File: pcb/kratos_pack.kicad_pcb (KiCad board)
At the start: 4 copper layers, 42.2 x 18.6 mm, 119 parts, among them J1 USB_C_Receptacle_USB2.0, J2 PROG_CONN_STM_6p, J3 DBG_UART, J5 BAT_7.4V, J6 BAT_0V, J7 OUT+, J8 OUT-, Q1 AON7403, Q2 AON7414, Q3 AON7414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

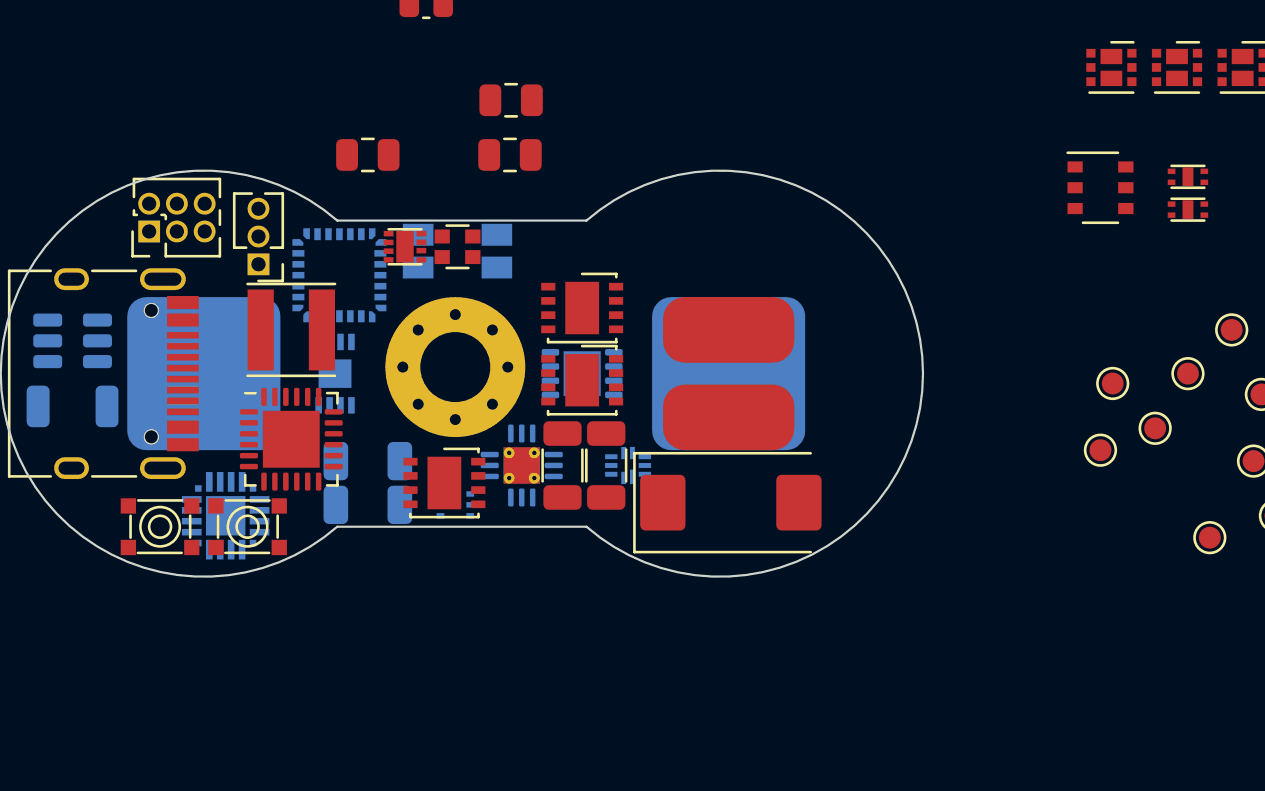
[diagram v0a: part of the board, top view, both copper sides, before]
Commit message: Schema: update footprint 3-pin connectors, project cleanup, add gitignore
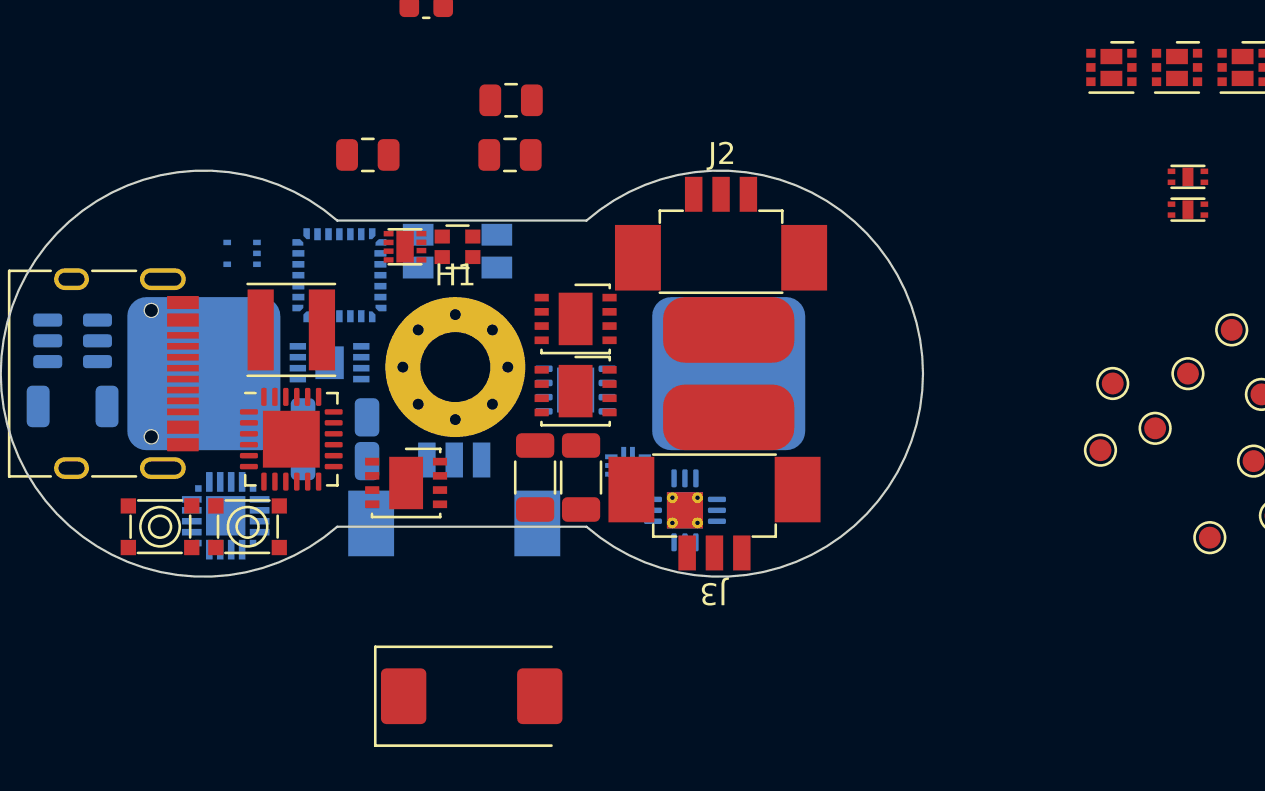
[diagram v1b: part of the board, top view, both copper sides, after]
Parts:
- removed U12: 74LVC2G14, Package_SO:TSOP-6_1.65x3.05mm_P0.95mm
- added J4: BAT_MID+NTC, TCY_connectors:Amphenol_10114828-11103LF_1x03_P1.25mm_Vertical, B.Cu at (151.4, 84.7)
- C22, C24: value 4.7uF(X7R) -> 4.7uF
- C23, C9: value 40nF -> 39nF
- J2: value PROG_CONN_STM_6p -> PROG_CONN; footprint Connector_PinHeader_1.27mm:PinHeader_2x03_P1.27mm_Vertical -> TCY_connectors:Amphenol_10114828-11103LF_1x03_P1.25mm_Vertical
- J3: footprint Connector_PinHeader_1.27mm:PinHeader_1x03_P1.27mm_Vertical -> TCY_connectors:Amphenol_10114828-11103LF_1x03_P1.25mm_Vertical
- moved J2 26.2 mm to (163.7, 72.5), turned to 0 degrees
- moved J3 24.3 mm to (163.3, 87.5)
- moved U6 15.1 mm to (141.8, 74.5)
- moved C17 14.8 mm to (152.2, 94.8)
- moved U8 7.74 mm to (162.0, 86.2)
- moved R23 2.50 mm to (146.0, 82.0)
- moved R24 2.50 mm to (146.0, 84.0)
- moved Q1 1.75 mm to (149.2, 85.0)
- moved R28 1.37 mm to (155.2, 84.8)
- moved R29 1.27 mm to (157.2, 84.8)
- moved U9 0.81 mm to (157.0, 80.8)
- moved Q2 0.58 mm to (157.0, 80.8)
- moved Q3 0.58 mm to (157.0, 77.5)
- moved U10 0.56 mm to (145.8, 79.5), turned to 0 degrees
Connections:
- J1 pad A8: no_connect_82 -> no_connect_81
- J1 pad B8: no_connect_83 -> no_connect_82
- J2 pad 2: +3V3 -> /SWCLK
- J2 pad 3: no_connect_84 -> /SWDIO
- Q4 pad 3: /DIV_1 -> /DIV_2
- Q5 pad 3: /DIV -> /DIV_1
- Q6 pad 3: /DIV_2 -> /DIV
- R16 pad 1: /DIV_2 -> /DIV
- R3 pad 1: /DIV_1 -> /DIV_2
- R8 pad 1: /DIV -> /DIV_1
- U2 pad 1: no_connect_85 -> no_connect_83
- U2 pad 10: no_connect_86 -> (no net)
- U2 pad 11: no_connect_87 -> no_connect_84
- U2 pad 14: no_connect_88 -> no_connect_85
- U2 pad 15: no_connect_89 -> no_connect_86
- U2 pad 16: no_connect_90 -> no_connect_87
- U2 pad 19: no_connect_91 -> no_connect_88
- U2 pad 2: no_connect_92 -> no_connect_89
- U2 pad 20: no_connect_93 -> no_connect_90
- U3 pad 1: no_connect_94 -> no_connect_91
- U3 pad 10: no_connect_95 -> no_connect_92
- U3 pad 11: no_connect_96 -> no_connect_93
- U3 pad 12: no_connect_97 -> no_connect_94
- U3 pad 13: no_connect_98 -> no_connect_95
- U3 pad 14: no_connect_99 -> no_connect_96
- U3 pad 15: no_connect_100 -> no_connect_97
- U3 pad 16: no_connect_101 -> no_connect_98
- U3 pad 17: no_connect_102 -> no_connect_99
- U3 pad 18: no_connect_103 -> no_connect_100
- U3 pad 19: no_connect_104 -> no_connect_101
- U3 pad 2: no_connect_105 -> no_connect_102
- U3 pad 20: no_connect_106 -> no_connect_103
- U3 pad 22: no_connect_107 -> no_connect_104
- U3 pad 23: no_connect_108 -> no_connect_105
- U3 pad 24: no_connect_109 -> no_connect_106
- U3 pad 25: no_connect_110 -> no_connect_107
- U3 pad 26: no_connect_111 -> no_connect_108
- U3 pad 27: no_connect_112 -> no_connect_109
- U3 pad 28: no_connect_113 -> no_connect_110
- U3 pad 6: no_connect_114 -> no_connect_111
- U3 pad 7: no_connect_115 -> no_connect_112
- U3 pad 8: no_connect_116 -> no_connect_113
- U3 pad 9: no_connect_117 -> no_connect_114
- U4 pad 1: no_connect_118 -> no_connect_115
- U7 pad 8: Net-(U7-Pad8) -> GND

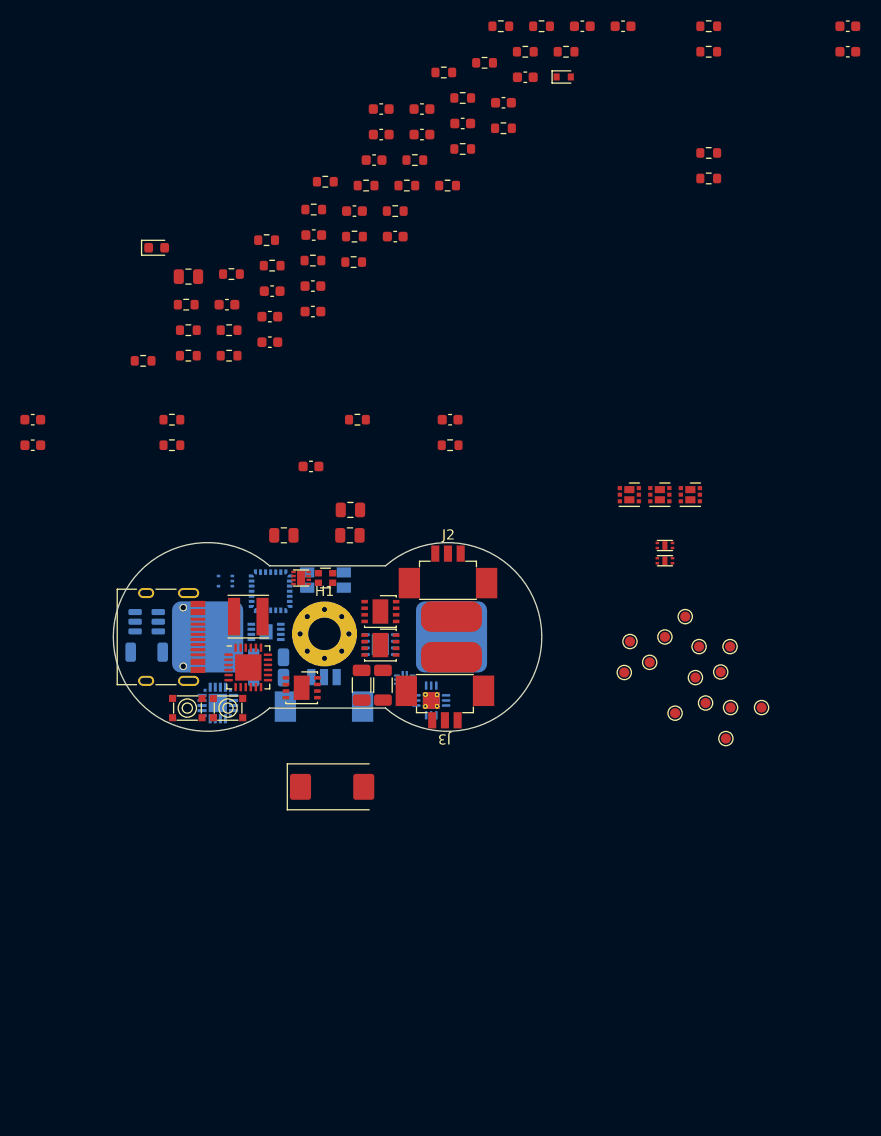
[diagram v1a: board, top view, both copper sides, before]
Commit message: PCB: Route USB input, charger circuit and switches
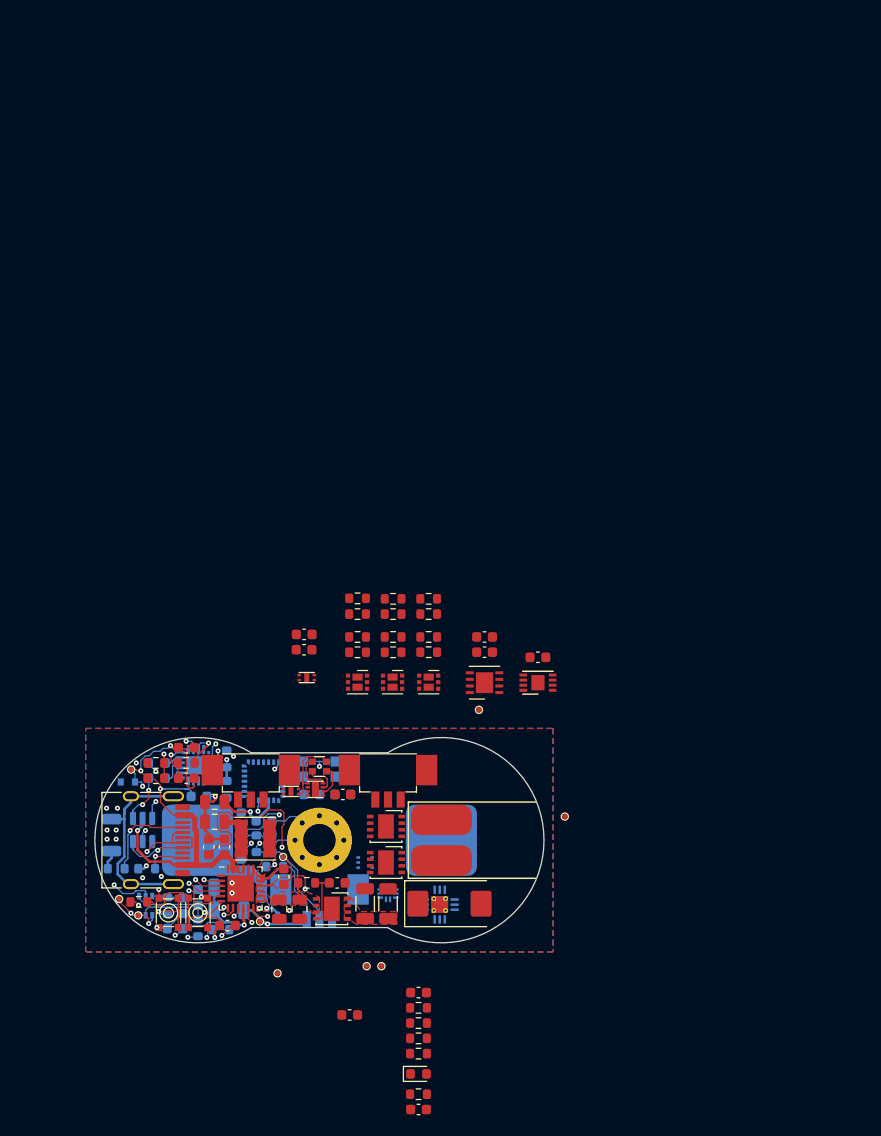
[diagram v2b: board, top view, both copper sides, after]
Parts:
- removed C15: 100nF, Capacitor_SMD:C_0603_1608Metric
- removed C2: 4.7uF, Capacitor_SMD:C_0603_1608Metric
- removed TP11, TP13: TestPoint, TestPoint:TestPoint_Pad_D1.0mm
- added U12: 74LVC2G14, Package_TO_SOT_SMD:SOT-363_SC-70-6, B.Cu at (133.9, 106.5)
- C1, C13, C27, C28, C29, C30, C4, D1, R1, R10, R11, R12, R13, R18, R2, R20, R21, R22, R35, R36, R5, R6: moved to B.Cu
- TP1, TP3: footprint TestPoint:TestPoint_Pad_D1.0mm -> TCY_connectors:TestPoint_Pad_D0.5mm; moved to B.Cu
- TP10, TP12, TP14, TP2, TP4, TP5, TP6, TP7, TP8, TP9: footprint TestPoint:TestPoint_Pad_D1.0mm -> TCY_connectors:TestPoint_Pad_D0.5mm
- U10, U9: moved to F.Cu
- moved R25 97.7 mm to (160.8, 121.0)
- moved C23 96.0 mm to (160.8, 126.5)
- moved C29 90.5 mm to (153.3, 95.5), turned to 180 degrees
- moved C30 90.1 mm to (150.2, 95.5)
- moved C5 89.8 mm to (141.7, 100.7), turned to 90 degrees
- moved C10 88.5 mm to (141.9, 108.4)
- moved R21 86.4 mm to (143.3, 101.1), turned to 90 degrees
- moved D3 85.3 mm to (160.8, 123.0)
- moved R19 84.2 mm to (133.2, 106.1)
- moved C3 83.6 mm to (137.9, 93.9)
- moved R32 82.1 mm to (160.8, 125.0)
- moved R14 82.1 mm to (134.9, 93.9)
- moved D1 81.6 mm to (132.2, 94.3), turned to 180 degrees
- moved R20 80.7 mm to (143.3, 98.1), turned to -90 degrees
- moved R15 80.1 mm to (134.9, 92.4), turned to 180 degrees
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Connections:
- Q5 pad 3: /DIV_1 -> /DIV
- Q6 pad 3: /DIV -> /DIV_1
- R16 pad 1: /DIV -> /DIV_1
- R35 pad 2: /WAKEUP -> /IN
- R36 pad 2: /BOOTL -> /IN_1
- R8 pad 1: /DIV_1 -> /DIV
- SW1 pad 2: /OUT -> /IN
- SW2 pad 2: /OUT_1 -> /IN_1
- TP12 pad 1: /OUT -> /WAKEUP
- TP14 pad 1: /OUT_1 -> /BOOTL
- TP2 pad 1: Net-(C2-Pad1) -> VBUS
- U2 pad 10: (no net) -> no_connect_116
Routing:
- net VBUS: track 0.00 -> 52.6 mm, vias 0 -> 5
- net GND: track 0.00 -> 51.7 mm, vias 0 -> 22
- net +3V3: track 0.00 -> 42.8 mm, vias 0 -> 2
- net /BOOTL: track 0.00 -> 28.7 mm, vias 0 -> 2
- net /IN: track 0.00 -> 28.4 mm, vias 0 -> 2
- net Net-(C8-Pad2): track 0.00 -> 27.4 mm, vias 0 -> 2
- net /USB_DET: track 0.00 -> 24.7 mm, vias 0 -> 3
- net /TS: track 0.00 -> 21.4 mm, vias 0 -> 2
- net Net-(FB1-Pad1): track 0.00 -> 19.9 mm
- net /RESET: track 0.00 -> 18.8 mm, vias 0 -> 2
- net /CH_STAT: track 0.00 -> 17.1 mm, vias 0 -> 2
- net /SCL: track 0.00 -> 16.9 mm, vias 0 -> 1
- net /CH_INT: track 0.00 -> 16.8 mm, vias 0 -> 1
- net /B1_V: track 0.00 -> 16.5 mm, vias 0 -> 1
- net /SDA: track 0.00 -> 14.4 mm, vias 0 -> 1
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- added copper zone on B.Cu, net /B2_V
- added copper zone on F.Cu, net /B2_V
- added copper zone on F.Cu, net /VBAT
- added copper zone on B.Cu, net GND
- added copper zone on F.Cu, net GND
- added copper zone on In1.Cu, net GND
- added copper zone on In2.Cu, net GND
- added copper zone on F.Cu, net Net-(C7-Pad1)
- added copper zone on F.Cu, net Net-(C9-Pad2)
- added copper zone on F.Cu, net VCC
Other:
- board size 42.2 x 18.6 mm -> 44.2 x 20.2 mm

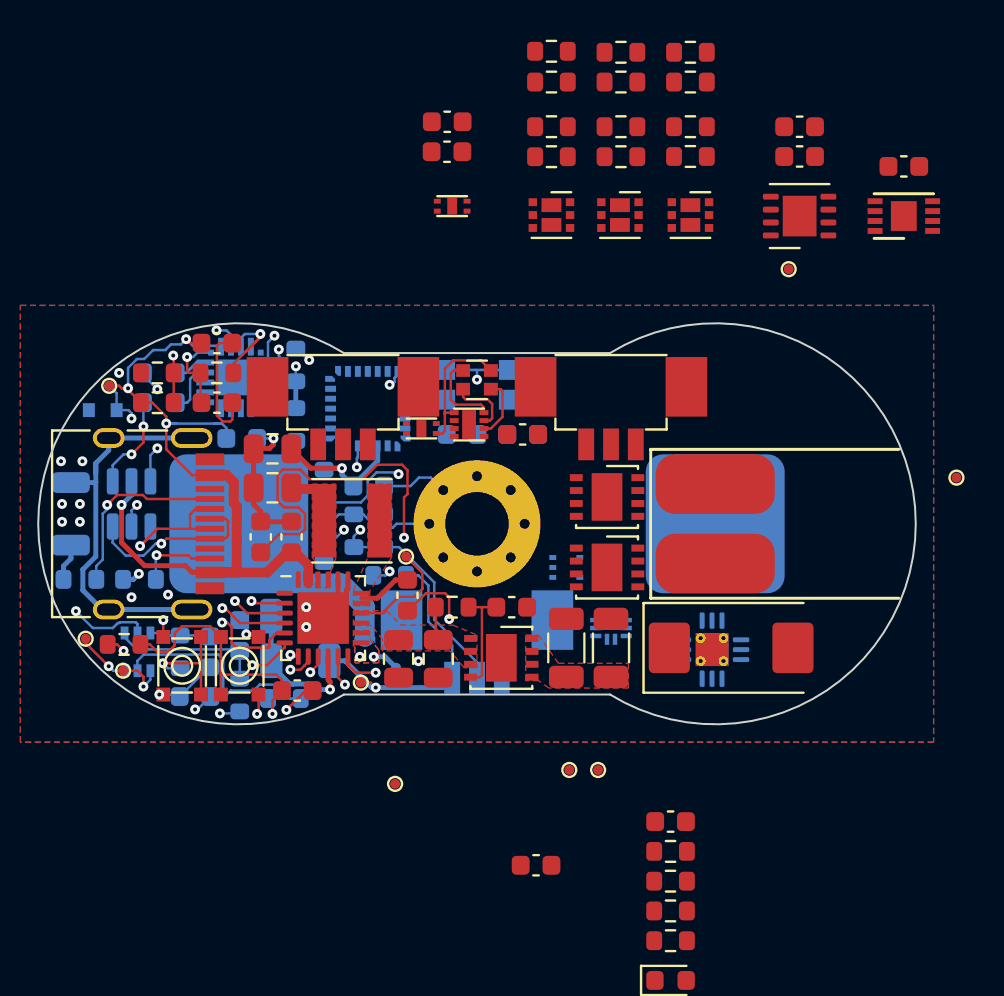
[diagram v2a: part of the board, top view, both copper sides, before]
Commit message: PCB: routing of mcu, voltage mesuring, part of current sensing and power regulator
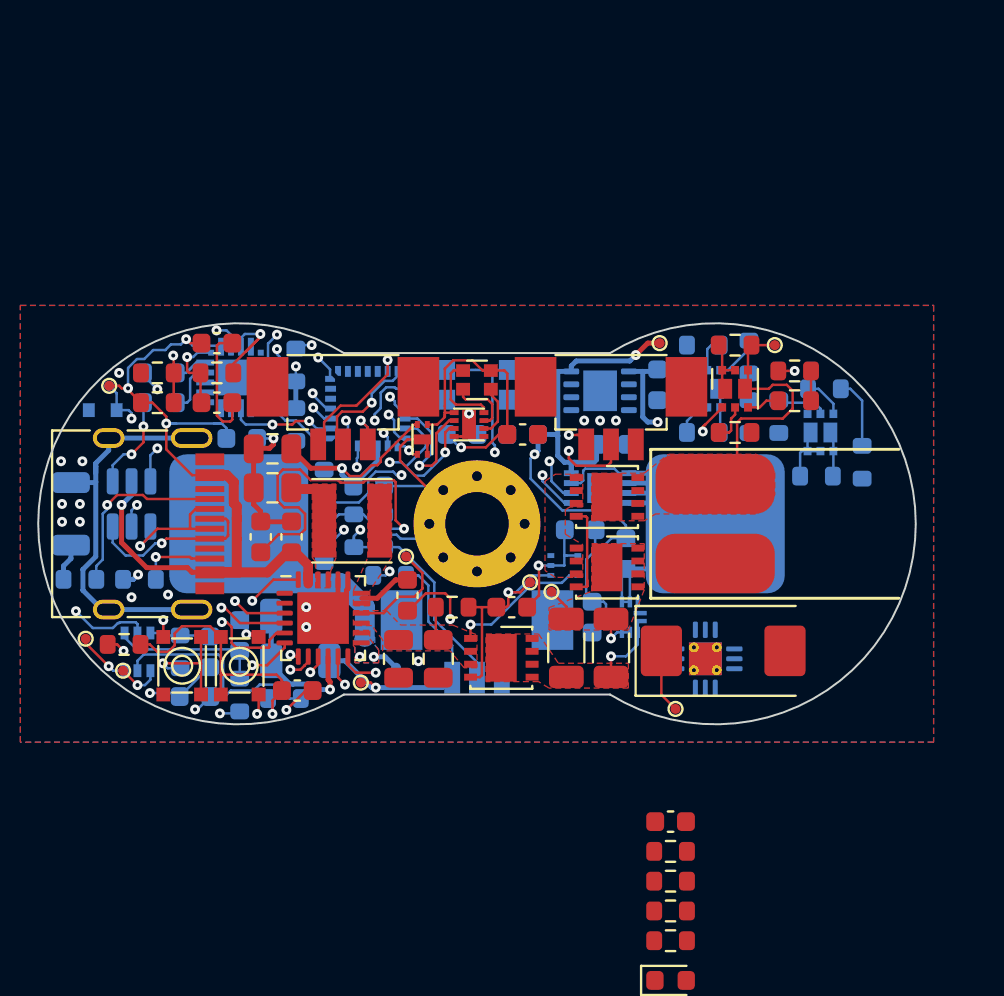
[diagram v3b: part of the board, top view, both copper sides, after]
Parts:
- C18, C21, C22, C24, C25, C26, Q4, Q5, R3, R33, R34, R37, R38, R4, R8, R9, U10, U11, U9: moved to B.Cu
- R20: value 470k -> 10k
- moved C25 23.5 mm to (158.5, 101.5), turned to -90 degrees
- moved R16 21.4 mm to (167.0, 93.8)
- moved R4 21.0 mm to (170.4, 96.9), turned to -90 degrees
- moved U10 20.5 mm to (157.2, 98.2)
- moved C21 20.3 mm to (157.8, 96.0)
- moved C26 20.2 mm to (156.2, 100.3), turned to 180 degrees
- moved U11 19.6 mm to (157.2, 102.1), turned to 90 degrees
- moved R17 19.0 mm to (167.0, 92.3), turned to 180 degrees
- moved R3 18.2 mm to (168.5, 93.2)
- moved R9 18.0 mm to (164.7, 94.6), turned to -90 degrees
- moved C24 17.3 mm to (154.3, 93.0), turned to -90 degrees
- moved R34 17.3 mm to (168.1, 97.6), turned to 180 degrees
- moved R8 16.7 mm to (164.7, 91.6), turned to -90 degrees
- moved R39 16.4 mm to (164.0, 95.4)
- moved R38 15.9 mm to (162.4, 95.4), turned to 180 degrees
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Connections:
- J1 pad A8: no_connect_81 -> no_connect_79
- J1 pad B8: no_connect_82 -> no_connect_80
- Q1 pad 9: (no net) -> VCC
- Q2 pad 9: (no net) -> /SENSE
- Q3 pad 9: (no net) -> /OUT_V
- Q4 pad 3: /DIV_2 -> /DIV_1
- Q5 pad 3: /DIV -> /DIV_2
- Q6 pad 3: /DIV_1 -> /DIV
- R16 pad 1: /DIV_1 -> /DIV
- R20 pad 1: +3V3 -> /PSEL
- R20 pad 2: /CH_STAT -> GND
- R3 pad 1: /DIV_2 -> /DIV_1
- R8 pad 1: /DIV -> /DIV_2
- U2 pad 1: no_connect_83 -> no_connect_81
- U2 pad 10: no_connect_116 -> no_connect_102
- U2 pad 11: no_connect_84 -> no_connect_82
- U2 pad 14: no_connect_85 -> no_connect_83
- U2 pad 15: no_connect_86 -> no_connect_84
- U2 pad 16: no_connect_87 -> no_connect_85
- U2 pad 17: /COM_RX -> /COM_TX
- U2 pad 18: /COM_TX -> /COM_RX
- U2 pad 19: no_connect_88 -> no_connect_86
- U2 pad 2: no_connect_89 -> no_connect_87
- U2 pad 20: no_connect_90 -> no_connect_88
- U3 pad 1: no_connect_91 -> /LED_EN
- U3 pad 10: no_connect_92 -> /WAKEUP
- U3 pad 11: no_connect_93 -> /DBG_TX
- U3 pad 12: no_connect_94 -> no_connect_89
- U3 pad 13: no_connect_95 -> no_connect_90
- U3 pad 14: no_connect_96 -> /DBG_RX
- U3 pad 15: no_connect_97 -> no_connect_91
- U3 pad 16: no_connect_98 -> no_connect_92
- U3 pad 17: no_connect_99 -> no_connect_93
- U3 pad 18: no_connect_100 -> no_connect_94
- U3 pad 19: no_connect_101 -> no_connect_95
- U3 pad 2: no_connect_102 -> /CD
- U3 pad 20: no_connect_103 -> /SWDIO
- U3 pad 21: /BOOTL -> /SWCLK
- U3 pad 22: no_connect_104 -> no_connect_96
- U3 pad 23: no_connect_105 -> /PSEL
- U3 pad 24: no_connect_106 -> no_connect_97
- U3 pad 25: no_connect_107 -> /USB_DET
- U3 pad 26: no_connect_108 -> /SCL
- U3 pad 27: no_connect_109 -> /SDA
- U3 pad 28: no_connect_110 -> /CH_INT
- U3 pad 6: no_connect_111 -> /BOOTL
- U3 pad 7: no_connect_112 -> no_connect_98
- U3 pad 8: no_connect_113 -> /COM_TX
- U3 pad 9: no_connect_114 -> /COM_RX
- U4 pad 1: no_connect_115 -> no_connect_99
- U5 pad 1: /PG -> no_connect_100
- U5 pad 2: /CH_STAT -> no_connect_101
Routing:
- net GND: track 51.7 -> 109.2 mm, vias 22 -> 30
- net +3V3: track 42.8 -> 84.2 mm, vias 2 -> 4
- net /PSEL: track 0.00 -> 25.8 mm, vias 0 -> 3
- net /WAKEUP: track 2.76 -> 24.0 mm, vias 1 -> 2
- net /SCL: track 16.9 -> 36.3 mm, vias 1 -> 3
- net /DBG_TX: track 0.00 -> 19.2 mm, vias 0 -> 2
- net /SDA: track 14.4 -> 31.8 mm, vias 1 -> 4
- net /DBG_RX: track 0.00 -> 17.1 mm, vias 0 -> 2
- net /CH_STAT: track 17.1 -> 0.00 mm, vias 2 -> 0
- net /OUT_V: track 0.00 -> 14.3 mm
- net VCC: track 0.00 -> 12.0 mm, vias 0 -> 2
- net /USB_DET: track 24.7 -> 32.5 mm, vias 3 -> 4
- net /LED_PWR: track 6.88 -> 14.3 mm, vias 0 -> 1
- net /VBAT: track 7.28 -> 14.4 mm, vias 0 -> 1
- net /SWDIO: track 0.00 -> 6.74 mm, vias 0 -> 1
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- added copper zone on F.Cu, net /OUT_V
- added copper zone on F.Cu, net /SENSE
- added copper zone on F.Cu, net Net-(Q2-Pad1)
